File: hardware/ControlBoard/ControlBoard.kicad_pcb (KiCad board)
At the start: 4 copper layers, 95 x 95 mm, 174 parts, among them J1 Lamp 1 Out, J10 CAN, J11 USB_B_Micro, J12 Conn_01x02, J13 Available GPIO, J14 MOTOR_CTRL1, J15 MOTOR_CTRL2, J2 ESTOP1, J3 ESTOP2, J4 Lamp 3 Out, J5 Lamp 2 Out, J6 Lamp 4 Out, J7 PWR_IN, J8 USB_B_Micro, J9 UART BACKUP, Q1 DMN62D0U-13, Q2 DMN62D0U-13, Q3 DMN62D0U-13, Q4 DMN62D0U-13, Q5 SS8050-G, Q6 SS8050-G, SW1 SW_Push, SW2 SW_Push, U1 CP2102N-A02-GQFN28, U10 74LVC1G17W5-7, U11 74LVC1G17W5-7, U12 TXU0104QPWRQ1, U2 Lora_Module, U3 L4941BV, U4 LD1086V33-DG, U5 ESP32-S3-WROOM-1U-N16, U6 74LVC1G97W6-7, U7 SN65HVD232, U8 SN74LVC1GU04DBVR, U9 TXU0104QPWRQ1

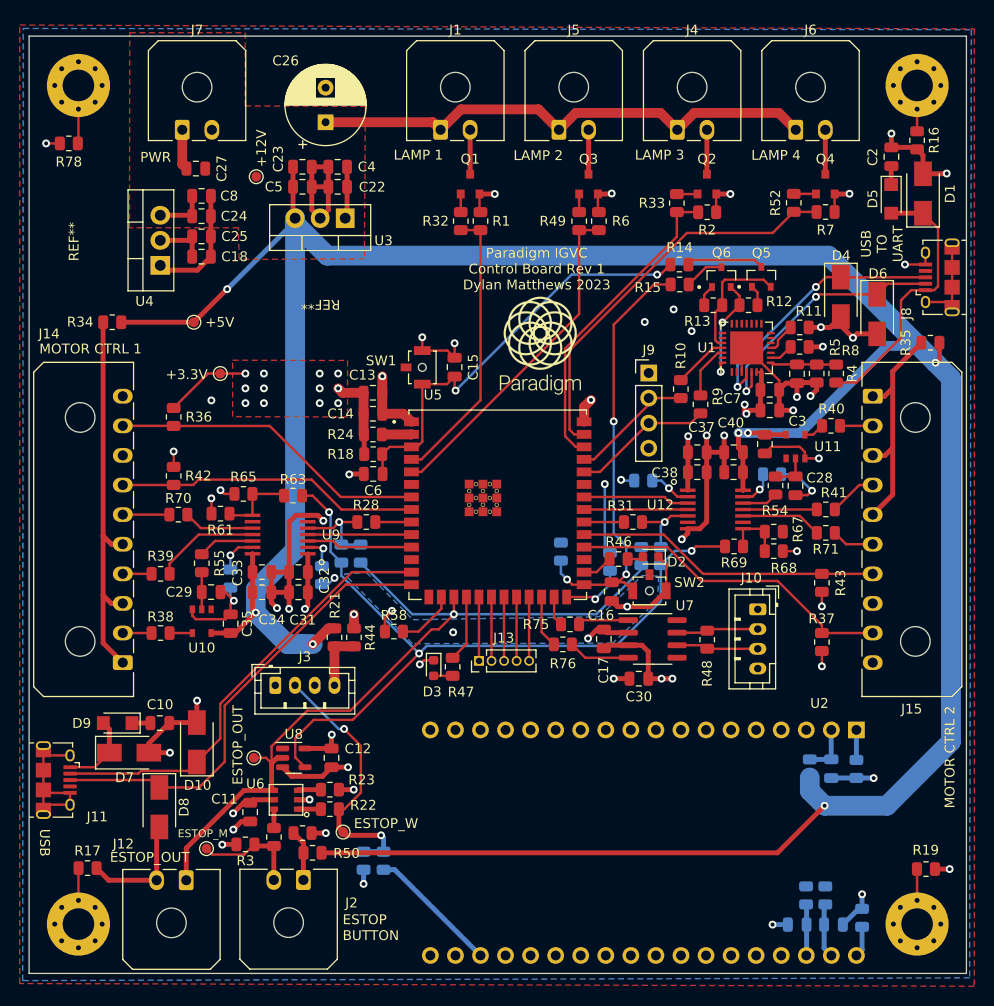
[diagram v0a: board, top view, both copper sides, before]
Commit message: Switch 5V LDO for DC DC
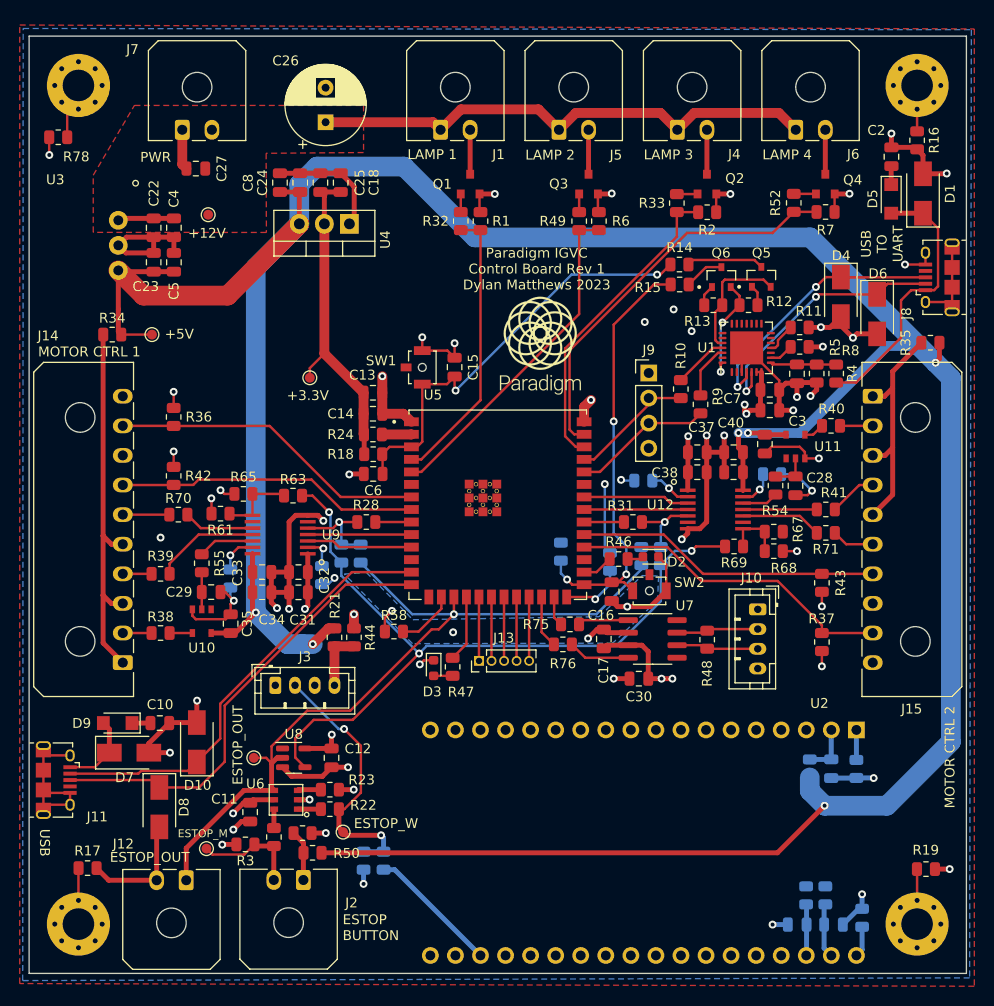
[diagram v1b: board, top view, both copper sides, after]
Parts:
- removed the REF** at (79.5, 76.7)
- C5: value 22u -> 10u
- R38, R39, R40, R41, R70, R71: value 0 -> 1k
- U3: value L4941BV -> R-78B5.0-2.0; footprint Package_TO_SOT_THT:TO-220-3_Vertical -> controlLib:R-78B5.0-2.0
- moved U3 26.2 mm to (56.0, 71.2), turned to -90 degrees
- moved REF** 25.8 mm to (80.0, 77.3), turned to 180 degrees
- moved U4 19.6 mm to (82.5, 69.0), turned to 180 degrees
- moved C22 19.1 mm to (62.6, 69.4), turned to 90 degrees
- moved C23 17.9 mm to (62.6, 72.9), turned to -90 degrees
- moved C4 17.7 mm to (64.7, 69.4), turned to 90 degrees
- moved C18 16.0 mm to (81.6, 64.8), turned to 90 degrees
- moved C5 15.1 mm to (64.7, 72.9), turned to 90 degrees
- moved C25 13.2 mm to (79.5, 64.8), turned to 90 degrees
- moved C24 10.6 mm to (77.5, 64.8), turned to -90 degrees
- moved TP3 9.08 mm to (78.5, 84.6)
- moved C8 8.06 mm to (75.4, 64.8), turned to -90 degrees
- moved TP1 6.21 mm to (68.2, 68.1)
- moved TP2 4.43 mm to (62.5, 80.2)
- moved R34 1.25 mm to (58.4, 80.2)
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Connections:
- C24 pad 2: +12V -> +5V
- C8 pad 2: +12V -> +5V
- U4 pad 3: +12V -> +5V
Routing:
- net +5V: track 306.9 -> 328.6 mm, vias 7 -> 6
- net +3V3: track 73.7 -> 85.7 mm, vias 29 -> 18
- net +12V: track 63.1 -> 58.2 mm
- net /DIR+_1_5V: track 40.0 -> 38.8 mm
- net GND: track 269.9 -> 269.0 mm
- removed copper zone on F.Cu, net +3V3

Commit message: Last things
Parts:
- added D11: S1G, Diode_SMD:D_SMA, F.Cu at (63.6, 81.8)
- added J16: 5V HEADER, Connector_Molex:Molex_KK-254_AE-6410-03A_1x03_P2.54mm_Vertical, F.Cu at (68.9, 79.6)
- moved TP2 7.77 mm to (54.9, 78.7)
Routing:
- net +5V: track 328.6 -> 340.6 mm
- net GND: track 269.0 -> 274.6 mm

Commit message: Finish adding assembly PNs
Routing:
- added copper zone on B.Cu, net +12V
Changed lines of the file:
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@@
     (pad "41_9" thru_hole circle (at -0.1 0.01) (size 0.45 0.45) (drill 0.3) (layers *.Cu)
       (net 2 "GND") (pinfunction "GND") (pintype "power_in"))
+    (model "${KIPRJMOD}/3D_lib/ESP32-S3-WROOM-1U--3DModel-STEP-56544.STEP"
+      (offset (xyz 0 0 0))
+      (scale (xyz 1 1 1))
+      (rotate (xyz -90 0 0))
+    )
   )
   (footprint "Button_Switch_SMD:SW_SPST_B3U-1100P-B" (layer "F.Cu")
@@
     )
   )
-  (zone (net 5) (net_name "+12V") (layer "F.Cu") (hatch edge 0.508)
-    (priority 1)
+  (zone (net 5) (net_name "+12V") (layers F&B.Cu) (hatch edge 0.508)
+    (priority 2)
     (connect_pads (clearance 0.508))
     (min_thickness 0.254) (filled_areas_thickness no)
